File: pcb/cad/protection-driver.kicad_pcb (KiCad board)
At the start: 2 copper layers, 120 x 80 mm, 52 parts, among them J1 Vdc, J2 contactor, J4 PS1, K1 G5V-2, Q1 BC337, Q2 TIP122, SW1 SW_Push_Dual_x2, SW2 SW_Push_Dual_x2, SW3 SW_SPST, SW4 Protect_sel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

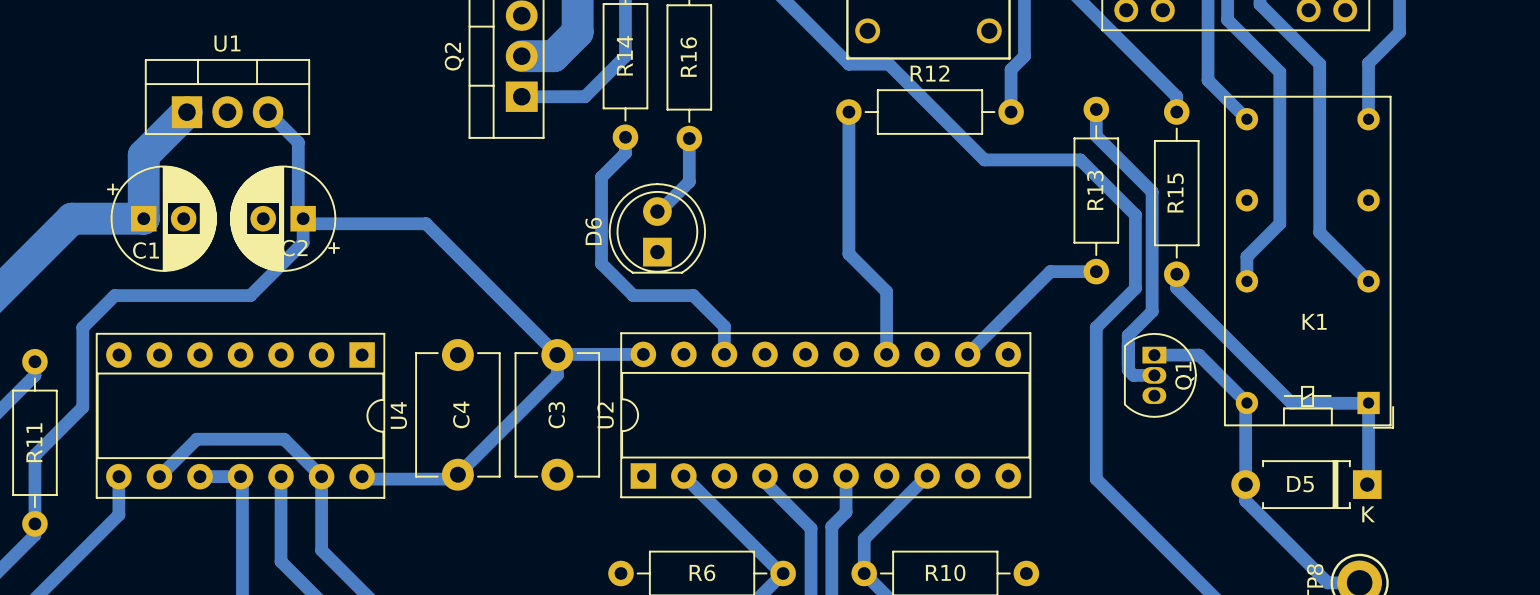
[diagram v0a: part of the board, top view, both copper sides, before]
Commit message: schematic formatting
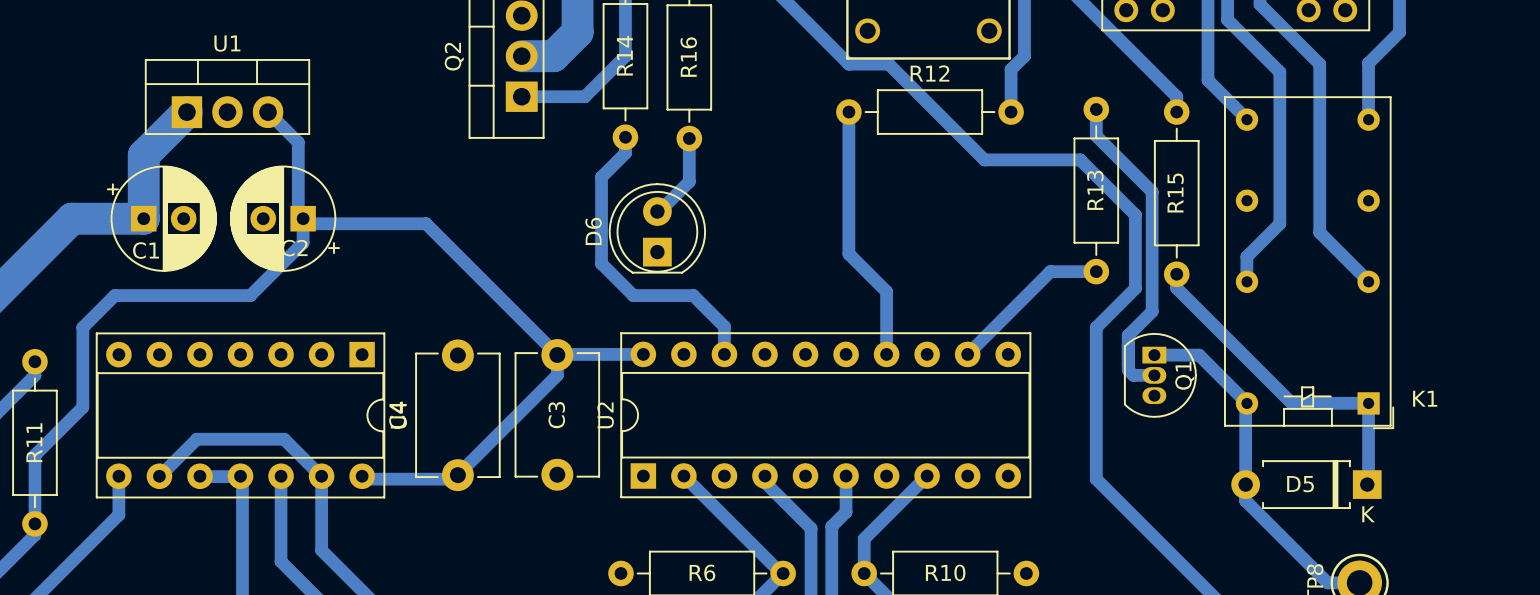
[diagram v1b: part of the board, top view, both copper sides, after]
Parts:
- K1: value G5V-2 -> ML2RC2
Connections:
- net /SR_Latch/R renamed /R
- net /SR_Latch/S renamed /S
- net /SR_Latch/~{Q} renamed /~{Q}

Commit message: Include driver for second contactor with delayed activation
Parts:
- J2: value contactor -> contactor_1
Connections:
- net /IGBT_on renamed /IGBT
- net /contactor_on renamed /contactor_1
- net /relay_on renamed /PS_interlock
- U2 pad 11: GND -> Net-(C6-Pad1)
- U2 pad 13: GND -> Net-(R19-Pad2)
- U2 pad 16: unconnected-(U2-Pad16) -> Net-(U2-Pad16)
- U2 pad 7: unconnected-(U2-Pad7) -> Net-(R17-Pad2)
- U2 pad 9: unconnected-(U2-Pad9) -> Net-(R20-Pad1)
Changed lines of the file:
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@@
   (net 21 "Net-(R7-Pad1)")
   (net 22 "/Q")
-  (net 23 "unconnected-(U2-Pad9)")
+  (net 23 "/IGBT")
   (net 24 "Net-(R9-Pad1)")
   (net 25 "Net-(R10-Pad1)")
-  (net 26 "/IGBT_on")
+  (net 26 "Net-(R12-Pad2)")
   (net 27 "/~{Q}")
-  (net 28 "/relay_on")
-  (net 29 "/contactor_on")
+  (net 28 "/PS_interlock")
+  (net 29 "/contactor_1")
   (net 30 "unconnected-(U2-Pad3)")
   (net 31 "unconnected-(U2-Pad5)")
-  (net 32 "unconnected-(U2-Pad7)")
+  (net 32 "Net-(R17-Pad2)")
   (net 33 "unconnected-(U3-Pad5)")
   (net 34 "unconnected-(U3-Pad8)")
@@
   (net 42 "Net-(J2-Pad1)")
   (net 43 "Net-(J2-Pad2)")
-  (net 44 "unconnected-(U2-Pad16)")
+  (net 44 "Net-(R20-Pad1)")
   (net 45 "/S")
   (net 46 "/R")
-  (net 47 "Net-(U3-Pad1)")
+  (net 47 "Net-(C6-Pad1)")
+  (net 48 "Net-(R19-Pad2)")
+  (net 49 "Net-(U2-Pad16)")
   (footprint "Resistor_THT:R_Axial_DIN0207_L6.3mm_D2.5mm_P10.16mm_Horizontal" (layer "F.Cu")
     (at 124.5 100.304 90)
@@
       (net 24 "Net-(R9-Pad1)") (pinfunction "1A2") (pintype "input"))
     (pad "7" thru_hole oval (at 0 15.24 90) (size 1.6 1.6) (drill 0.8) (layers *.Cu *.Mask)
-      (net 32 "unconnected-(U2-Pad7)") (pinfunction "2Y2") (pintype "tri_state"))
+      (net 32 "Net-(R17-Pad2)") (pinfunction "2Y2") (pintype "tri_state"))
     (pad "8" thru_hole oval (at 0 17.78 90) (size 1.6 1.6) (drill 0.8) (layers *.Cu *.Mask)
       (net 25 "Net-(R10-Pad1)") (pinfunction "1A3") (pintype "input"))
     (pad "9" thru_hole oval (at 0 20.32 90) (size 1.6 1.6) (drill 0.8) (layers *.Cu *.Mask)
-      (net 23 "unconnected-(U2-Pad9)") (pinfunction "2Y3") (pintype "tri_state"))
+      (net 44 "Net-(R20-Pad1)") (pinfunction "2Y3") (pintype "tri_state"))
     (pad "10" thru_hole oval (at 0 22.86 90) (size 1.6 1.6) (drill 0.8) (layers *.Cu *.Mask)
       (net 2 "GND") (pinfunction "GND") (pintype "power_in"))
     (pad "11" thru_hole oval (at 7.62 22.86 90) (size 1.6 1.6) (drill 0.8) (layers *.Cu *.Mask)
-      (net 2 "GND") (pinfunction "2A3") (pintype "input"))
+      (net 47 "Net-(C6-Pad1)") (pinfunction "2A3") (pintype "input"))
     (pad "12" thru_hole oval (at 7.62 20.32 90) (size 1.6 1.6) (drill 0.8) (layers *.Cu *.Mask)
-      (net 28 "/relay_on") (pinfunction "1Y3") (pintype "tri_state"))
+      (net 28 "/PS_interlock") (pinfunction "1Y3") (pintype "tri_state"))
     (pad "13" thru_hole oval (at 7.62 17.78 90) (size 1.6 1.6) (drill 0.8) (layers *.Cu *.Mask)
-      (net 2 "GND") (pinfunction "2A2") (pintype "input"))
+      (net 48 "Net-(R19-Pad2)") (pinfunction "2A2") (pintype "input"))
     (pad "14" thru_hole oval (at 7.62 15.24 90) (size 1.6 1.6) (drill 0.8) (layers *.Cu *.Mask)
-      (net 26 "/IGBT_on") (pinfunction "1Y2") (pintype "tri_state"))
+      (net 23 "/IGBT") (pinfunction "1Y2") (pintype "tri_state"))
     (pad "15" thru_hole oval (at 7.62 12.7 90) (size 1.6 1.6) (drill 0.8) (layers *.Cu *.Mask)
       (net 2 "GND") (pinfunction "2A1") (pintype "input"))
     (pad "16" thru_hole oval (at 7.62 10.16 90) (size 1.6 1.6) (drill 0.8) (layers *.Cu *.Mask)
-      (net 44 "unconnected-(U2-Pad16)") (pinfunction "1Y1") (pintype "tri_state"))
+      (net 49 "Net-(U2-Pad16)") (pinfunction "1Y1") (pintype "tri_state"))
     (pad "17" thru_hole oval (at 7.62 7.62 90) (size 1.6 1.6) (drill 0.8) (layers *.Cu *.Mask)
       (net 2 "GND") (pinfunction "2A0") (pintype "input"))
     (pad "18" thru_hole oval (at 7.62 5.08 90) (size 1.6 1.6) (drill 0.8) (layers *.Cu *.Mask)
-      (net 29 "/contactor_on") (pinfunction "1Y0") (pintype "tri_state"))
+      (net 29 "/contactor_1") (pinfunction "1Y0") (pintype "tri_state"))
     (pad "19" thru_hole oval (at 7.62 2.54 90) (size 1.6 1.6) (drill 0.8) (layers *.Cu *.Mask)
       (net 2 "GND") (pinfunction "2OE") (pintype "input"))
@@
     (fp_line (start 1.93 1.25) (end 8.23 1.25) (layer "F.Fab") (width 0.1))
     (pad "1" thru_hole circle (at 0 0 90) (size 1.6 1.6) (drill 0.8) (layers *.Cu *.Mask)
-      (net 29 "/contactor_on") (pintype "passive"))
+      (net 29 "/contactor_1") (pintype "passive"))
     (pad "2" thru_hole oval (at 10.16 0 90) (size 1.6 1.6) (drill 0.8) (layers *.Cu *.Mask)
       (net 18 "Net-(Q2-Pad1)") (pintype "passive"))
@@
       (effects (font (size 1 1) (thickness 0.15)))
     )
-    (fp_text value "contactor" (at 5.72 4.2) (layer "F.Fab")
+    (fp_text value "contactor_1" (at 5.72 4.2) (layer "F.Fab")
       (effects (font (size 1 1) (thickness 0.15)))
     )
@@
     (fp_line (start 10.16 0) (end 8.23 0) (layer "F.Fab") (width 0.1))
     (pad "1" thru_hole circle (at 0 0 90) (size 1.6 1.6) (drill 0.8) (layers *.Cu *.Mask)
-      (net 28 "/relay_on") (pintype "passive"))
+      (net 28 "/PS_interlock") (pintype "passive"))
     (pad "2" thru_hole oval (at 10.16 0 90) (size 1.6 1.6) (drill 0.8) (layers *.Cu *.Mask)
       (net 17 "Net-(Q1-Pad2)") (pintype "passive"))
@@
     (pad "" np_thru_hole circle (at -1.014999 3.605) (size 2.25 2.25) (drill 2.25) (layers *.Cu *.Mask))
     (pad "1" thru_hole rect (at 2.795 -0.205) (size 1.56 1.56) (drill 1.01) (layers *.Cu *.Mask)
-      (net 47 "Net-(U3-Pad1)") (pinfunction "Anode") (pintype "passive"))
+      (net 26 "Net-(R12-Pad2)") (pinfunction "Anode") (pintype "passive"))
     (pad "2" thru_hole circle (at 0.255 -0.205) (size 1.56 1.56) (drill 1.01) (layers *.Cu *.Mask)
       (net 2 "GND") (pinfunction "Cathode") (pintype "passive"))
@@
     (fp_line (start 1.93 1.25) (end 8.23 1.25) (layer "F.Fab") (width 0.1))
     (pad "1" thru_hole circle (at 0 0) (size 1.6 1.6) (drill 0.8) (layers *.Cu *.Mask)
-      (net 26 "/IGBT_on") (pintype "passive"))
+      (net 23 "/IGBT") (pintype "passive"))
     (pad "2" thru_hole oval (at 10.16 0) (size 1.6 1.6) (drill 0.8) (layers *.Cu *.Mask)
-      (net 47 "Net-(U3-Pad1)") (pintype "passive"))
+      (net 26 "Net-(R12-Pad2)") (pintype "passive"))
     (model "${KICAD6_3DMODEL_DIR}/Resistor_THT.3dshapes/R_Axial_DIN0207_L6.3mm_D2.5mm_P10.16mm_Horizontal.wrl"
       (offset (xyz 0 0 0))
@@
   (segment (start 150 106.5) (end 147 106.5) (width 0.8) (layer "B.Cu") (net 22))
   (segment (start 142.433 97.371) (end 142.46 97.344) (width 0.8) (layer "B.Cu") (net 22))
+  (segment (start 175.5 83.393) (end 175.5 74.5) (width 0.8) (layer "B.Cu") (net 23))
+  (segment (start 177.861 85.754) (end 175.5 83.393) (width 0.8) (layer "B.Cu") (net 23))
+  (segment (start 177.861 89.686) (end 177.861 85.754) (width 0.8) (layer "B.Cu") (net 23))
   (segment (start 176.459 107.476) (end 174.427 105.444) (width 0.8) (layer "B.Cu") (net 24))
   (segment (start 175.321 99.5705) (end 175.321 97.306) (width 0.8) (layer "B.Cu") (net 24))
@@
   (segment (start 183.063 114.08) (end 183.063 113.572) (width 0.8) (layer "B.Cu") (net 25))
   (segment (start 176.459 103.412) (end 176.459 101.248) (width 0.8) (layer "B.Cu") (net 25))
-  (segment (start 175.5 83.393) (end 175.5 74.5) (width 0.8) (layer "B.Cu") (net 26))
-  (segment (start 177.861 85.754) (end 175.5 83.393) (width 0.8) (layer "B.Cu") (net 26))
-  (segment (start 177.861 89.686) (end 177.861 85.754) (width 0.8) (layer "B.Cu") (net 26))
+  (segment (start 186.5 67) (end 184.295 64.795) (width 0.8) (layer "B.Cu") (net 26))
+  (segment (start 185.66 71.84) (end 186.5 71) (width 0.8) (layer "B.Cu") (net 26))
+  (segment (start 186.5 71) (end 186.5 67) (width 0.8) (layer "B.Cu") (net 26))
+  (segment (start 184.295 64.795) (end 184.295 61.795) (width 0.8) (layer "B.Cu") (net 26))
+  (segment (start 185.66 74.5) (end 185.66 71.84) (width 0.8) (layer "B.Cu") (net 26))
   (segment (start 135.775 106.735) (end 137.5 105.01) (width 0.8) (layer "B.Cu") (net 27))
   (segment (start 137.457 97.344) (end 134.917 97.344) (width 0.8) (layer "B.Cu") (net 27))
@@
   (segment (start 127.652 115.5) (end 127.5 115.652) (width 0.8) (layer "B.Cu") (net 46))
   (segment (start 132.5 115.5) (end 139 115.5) (width 0.8) (layer "B.Cu") (net 46))
-  (segment (start 186.5 67) (end 184.295 64.795) (width 0.8) (layer "B.Cu") (net 47))
-  (segment (start 185.66 71.84) (end 186.5 71) (width 0.8) (layer "B.Cu") (net 47))
-  (segment (start 186.5 71) (end 186.5 67) (width 0.8) (layer "B.Cu") (net 47))
-  (segment (start 184.295 64.795) (end 184.295 61.795) (width 0.8) (layer "B.Cu") (net 47))
-  (segment (start 185.66 74.5) (end 185.66 71.84) (width 0.8) (layer "B.Cu") (net 47))
   (zone (net 2) (net_name "GND") (layer "B.Cu") (hatch edge 0.508)
     (connect_pads (clearance 0.25))
